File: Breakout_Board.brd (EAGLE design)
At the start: 100 x 80 mm, 93 parts, among them IC101 AD8620R, IC102 AD8620R, IC103 ADE7880, IC104 RH/H6, IC105 7805TV, Q101 16M384, U101 ADR512ARTZ-REEL7, U102 SI8640BD-B-IS, U103 SI8641BD-B-IS, X1 231-538/001-000, X101 STL266-04, X103 MKDSN1,5/2-5,08

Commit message: Board layout updated
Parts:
- moved R4 97.7 mm to (21.6, 70.6)
- moved R5 94.2 mm to (38.4, 51.3), turned to 180 degrees
- moved R1 89.8 mm to (10.7, 71.4), turned to 270 degrees
- moved R3 89.1 mm to (16.8, 70.6), turned to 180 degrees
- moved C2 85.0 mm to (49.8, 41.9), turned to 270 degrees
- moved R2 83.2 mm to (42.9, 42.2)
- moved X103 59.3 mm to (96.0, 16.8), turned to 270 degrees
- moved C102 30.5 mm to (17.8, 46.0), turned to 270 degrees
- moved R121 30.4 mm to (20.3, 40.4)
- moved C103 29.5 mm to (25.4, 44.5), turned to 270 degrees
- moved R112 25.4 mm to (16.0, 40.4), turned to 180 degrees
- moved R106 25.2 mm to (10.4, 40.9)
- moved C109 20.3 mm to (49.5, 21.6)
- moved R127 18.8 mm to (42.9, 23.6), turned to 270 degrees
- moved C105 18.4 mm to (17.8, 64.8), turned to 270 degrees
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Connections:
- net IAN: now also C2.2, R1.2, R3.2, X1.L2; no longer C109.2, R106.1, R112.2, X1.L8
- net IAP: now also C2.1, R2.2; no longer C109.1, R127.2
- net IBN: now also C107.2, R104.2, R110.2, X1.L3; no longer C108.2, R105.1, R111.2, X1.L6
- net IBP: now also C107.1, R125.2; no longer C108.1, R126.2
- net ICN: now also C108.2, R105.2, R111.2, X1.L6; no longer C107.2, R104.1, R110.2, X1.L4
- net ICP: now also C108.1, R126.2; no longer C107.1, R125.2
- net INN: now also C109.2, R106.1, R112.2, X1.L7; no longer C2.2, R1.1, R3.2, X1.L2
- net INP: now also C109.1, R127.2; no longer C2.1, R2.2
- net IN_I1: now also IC102.3, R104.1, X1.L4; no longer IC101.3, R104.2, X1.L3
- net IN_I2: now also R105.1; no longer R105.2
- net IN_I3: now also IC101.3, X1.L8; no longer IC102.3, X1.L7
- net N$18: now also IC101.1; no longer IC102.1
- net N$19: now also IC102.2; no longer IC101.2
- net N$21: now also IC102.1; no longer IC101.1
- net N$23: now also R1.1; no longer R1.2
- net N$29: now also IC101.2; no longer IC102.2
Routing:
- net VCC: track 48.7 -> 129.1 mm, vias 0 -> 3
- net INN: track 0.00 -> 63.5 mm, vias 0 -> 2
- net ICN: track 2.96 -> 62.3 mm, vias 0 -> 2
- net IAN: track 16.1 -> 70.2 mm, vias 0 -> 2
- net GND: track 37.7 -> 90.6 mm, vias 0 -> 5
- net N$22: track 0.00 -> 50.3 mm, vias 0 -> 2
- net IBN: track 25.7 -> 72.2 mm, vias 0 -> 2
- net N$21: track 2.28 -> 43.7 mm, vias 0 -> 2
- net GND_P: track 63.7 -> 24.4 mm, vias 0 -> 3
- net N$16: track 4.38 -> 41.3 mm, vias 0 -> 2
- net N$18: track 7.00 -> 40.9 mm, vias 0 -> 2
- net VCC_P: track 41.9 -> 10.5 mm, vias 0 -> 2
- net IN_I2: track 0.00 -> 24.5 mm
- net N$46: track 23.5 -> 0.00 mm
- net N$23: track 0.00 -> 22.7 mm, vias 0 -> 2
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- added copper zone on layer 1, net VCC
- added copper zone on layer 1, net VEE

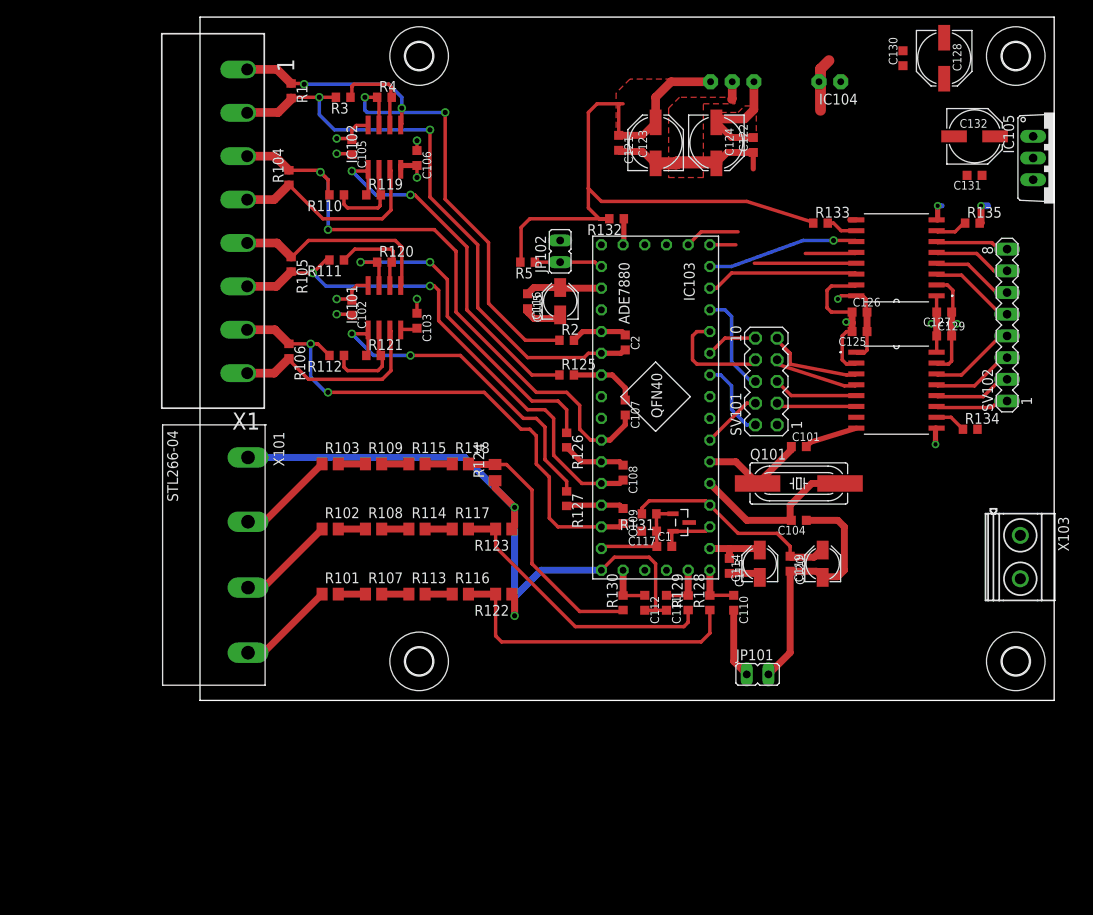
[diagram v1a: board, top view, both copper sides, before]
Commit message: Board layout finished without checking DRC
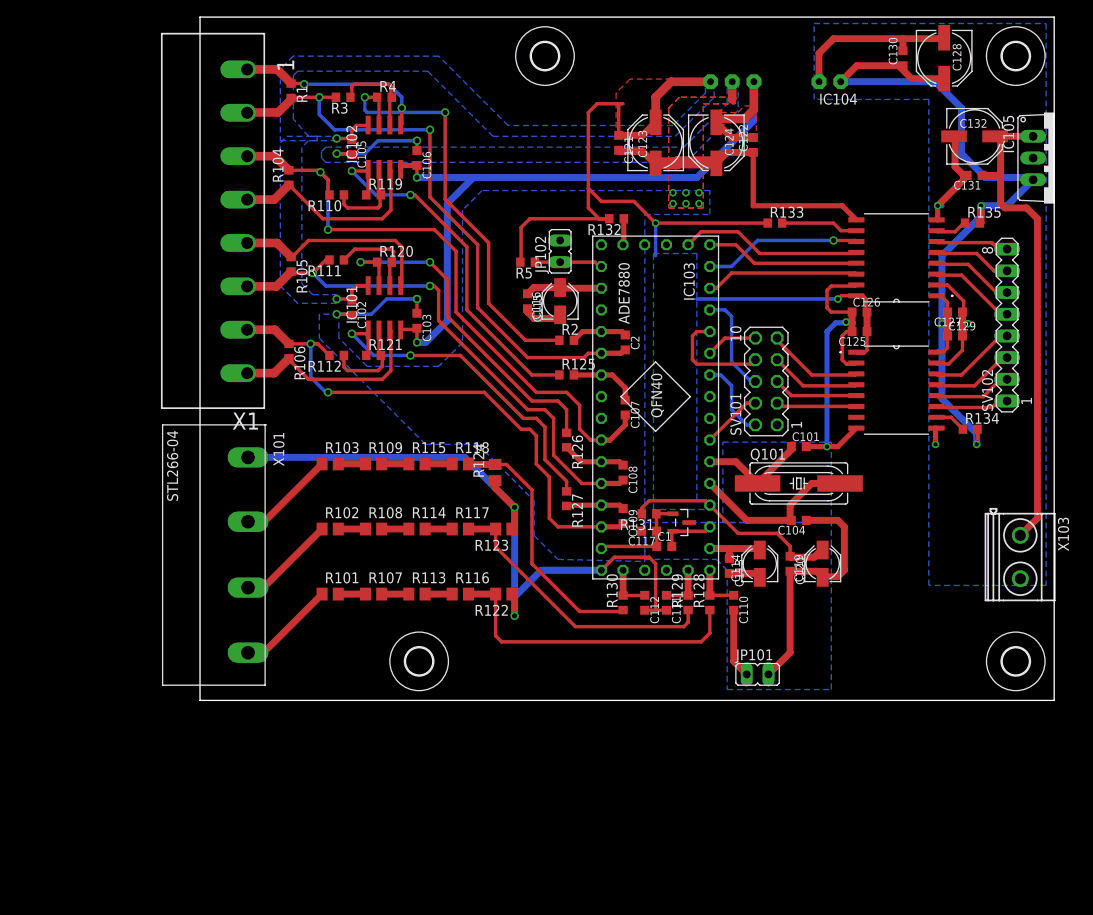
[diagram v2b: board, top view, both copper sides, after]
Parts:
- moved U$3 14.7 mm to (40.4, 75.4)
- moved R133 5.33 mm to (67.3, 55.9)
- moved C127 1.27 mm to (88.4, 45.5)
- moved C129 1.27 mm to (88.4, 42.7)
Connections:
- net GND: now also C117.2
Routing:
- net VCC_P: track 10.5 -> 96.8 mm, vias 2 -> 3
- net VEE: track 19.5 -> 90.3 mm, vias 1 -> 2
- net N$46: track 0.00 -> 57.5 mm
- net GND: track 90.6 -> 142.9 mm, vias 5 -> 12
- net GND_P: track 24.4 -> 48.9 mm
- net VCC: track 129.1 -> 144.4 mm, vias 3 -> 4
- net !SS: track 12.5 -> 21.4 mm
- net N$42: track 3.71 -> 9.04 mm
- net MOSI: track 15.0 -> 18.0 mm
- net MISO: track 17.7 -> 18.5 mm
- added copper zone on layer 16, net GND
- added copper zone on layer 16, net GND_P
- added copper zone on layer 16, net VCC

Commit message: First official release!
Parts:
- R1, R104, R105, R106: value 0R01 -> 4R7
- R110, R111, R112, R3: value 150R -> 6k49
- R119, R120, R121, R4: value 221k -> 2k21
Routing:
- net VN: track 90.7 -> 104.3 mm, vias 2 -> 3
- net GND: track 142.9 -> 136.6 mm
- net N$9: track 33.3 -> 35.8 mm
- net GND_P: vias 3 -> 8
- added copper zone on layer 1, net GND_P
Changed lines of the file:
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@@
 </class>
 <class number="1" name="HighU" width="0" drill="0">
-<clearance class="0" value="2"/>
+<clearance class="0" value="0.0254"/>
 </class>
 <class number="2" name="HIghI" width="0" drill="0">
-<clearance class="0" value="2"/>
+<clearance class="0" value="0.0254"/>
 <clearance class="1" value="2"/>
 </class>
@@
 </class>
 </classes>
-<designrules name="platinenbelichter">
+<designrules name="platinenbelichter *">
 <description language="de">&lt;b&gt;EAGLE Design Rules&lt;/b&gt;
 &lt;p&gt;
@@
 <param name="mtCopper" value="0.035mm 0.035mm 0.035mm 0.035mm 0.035mm 0.035mm 0.035mm 0.035mm 0.035mm 0.035mm 0.035mm 0.035mm 0.035mm 0.035mm 0.035mm 0.035mm"/>
 <param name="mtIsolate" value="1.5mm 0.15mm 0.2mm 0.15mm 0.2mm 0.15mm 0.2mm 0.15mm 0.2mm 0.15mm 0.2mm 0.15mm 0.2mm 0.15mm 0.2mm"/>
-<param name="mdWireWire" value="0.5mm"/>
-<param name="mdWirePad" value="0.5mm"/>
-<param name="mdWireVia" value="0.5mm"/>
-<param name="mdPadPad" value="0.5mm"/>
-<param name="mdPadVia" value="0.5mm"/>
-<param name="mdViaVia" value="0.5mm"/>
+<param name="mdWireWire" value="6mil"/>
+<param name="mdWirePad" value="6mil"/>
+<param name="mdWireVia" value="6mil"/>
+<param name="mdPadPad" value="6mil"/>
+<param name="mdPadVia" value="6mil"/>
+<param name="mdViaVia" value="6mil"/>
 <param name="mdSmdPad" value="0mil"/>
 <param name="mdSmdVia" value="0mil"/>
@@
 <element name="R124" library="rcl" package="R0805" value="1k" x="34.544" y="26.67" rot="R90"/>
 <element name="R130" library="rcl" package="R0603" value="1k" x="49.53" y="11.43" rot="R90"/>
-<element name="R104" library="rcl" package="R0603" value="0R01" x="10.414" y="61.214" rot="R90"/>
+<element name="R104" library="rcl" package="R0603" value="4R7" x="10.414" y="61.214" rot="R90"/>
 <element name="R107" library="rcl" package="R0805" value="162k" x="20.32" y="12.446"/>
 <element name="R125" library="rcl" package="R0603" value="1k" x="42.926" y="38.1"/>
-<element name="R110" library="rcl" package="R0603" value="150R" x="16.002" y="59.182" rot="R180"/>
-<element name="R119" library="rcl" package="R0603" value="221k" x="20.32" y="59.182"/>
-<element name="R105" library="rcl" package="R0603" value="0R01" x="10.668" y="51.054" rot="R270"/>
+<element name="R110" library="rcl" package="R0603" value="6k49" x="16.002" y="59.182" rot="R180"/>
+<element name="R119" library="rcl" package="R0603" value="2k21" x="20.32" y="59.182"/>
+<element name="R105" library="rcl" package="R0603" value="4R7" x="10.668" y="51.054" rot="R270"/>
 <element name="R126" library="rcl" package="R0603" value="1k" x="42.926" y="30.48" rot="R270"/>
-<element name="R111" library="rcl" package="R0603" value="150R" x="16.002" y="51.562" rot="R180"/>
-<element name="R120" library="rcl" package="R0603" value="221k" x="21.59" y="51.308"/>
-<element name="R106" library="rcl" package="R0603" value="0R01" x="10.414" y="40.894" rot="R270"/>
+<element name="R111" library="rcl" package="R0603" value="6k49" x="16.002" y="51.562" rot="R180"/>
+<element name="R120" library="rcl" package="R0603" value="2k21" x="21.59" y="51.308"/>
+<element name="R106" library="rcl" package="R0603" value="4R7" x="10.414" y="40.894" rot="R270"/>
 <element name="R127" library="rcl" package="R0603" value="1k" x="42.926" y="23.622" rot="R270"/>
-<element name="R112" library="rcl" package="R0603" value="150R" x="16.002" y="40.386" rot="R180"/>
+<element name="R112" library="rcl" package="R0603" value="6k49" x="16.002" y="40.386" rot="R180"/>
 <element name="R113" library="rcl" package="R0805" value="196k" x="25.4" y="12.446"/>
-<element name="R121" library="rcl" package="R0603" value="221k" x="20.32" y="40.386"/>
+<element name="R121" library="rcl" package="R0603" value="2k21" x="20.32" y="40.386"/>
 <element name="R132" library="rcl" package="R0603" value="10k" x="48.768" y="56.388" rot="R180"/>
 <element name="R131" library="rcl" package="R0603" value="2k1" x="52.578" y="21.844" rot="R180"/>
@@
 <element name="U$3" library="holes" package="3,2" value="" x="40.386" y="75.438"/>
 <element name="U$4" library="holes" package="3,2" value="" x="95.504" y="75.438"/>
-<element name="R1" library="rcl" package="R0603" value="0R01" x="10.668" y="71.374" rot="R270"/>
+<element name="R1" library="rcl" package="R0603" value="4R7" x="10.668" y="71.374" rot="R270"/>
 <element name="R2" library="rcl" package="R0603" value="1k" x="42.926" y="42.164"/>
 <element name="C2" library="rcl" package="C0603K" value="2n2" x="49.784" y="41.91" rot="R270"/>
-<element name="R3" library="rcl" package="R0603" value="150R" x="16.764" y="70.612" rot="R180"/>
-<element name="R4" library="rcl" package="R0603" value="221k" x="21.59" y="70.612"/>
+<element name="R3" library="rcl" package="R0603" value="6k49" x="16.764" y="70.612" rot="R180"/>
+<element name="R4" library="rcl" package="R0603" value="2k21" x="21.59" y="70.612"/>
 <element name="X1" library="con-wago_5.08mm" package="P-231-538/001-000" value="231-538/001-000" x="1.524" y="56.134" rot="R180"/>
 <element name="R5" library="rcl" package="R0603" value="10k" x="38.354" y="51.308" rot="R180"/>
@@
 <wire x1="31.43" y1="20.066" x2="34.61" y2="20.066" width="0.8128" layer="1"/>
 <wire x1="34.61" y1="20.066" x2="34.61" y2="17.968" width="0.4064" layer="1"/>
-<wire x1="34.61" y1="17.968" x2="43.942" y2="8.636" width="0.4064" layer="1"/>
-<wire x1="43.942" y1="8.636" x2="56.642" y2="8.636" width="0.4064" layer="1"/>
-<wire x1="56.642" y1="8.636" x2="57.15" y2="9.144" width="0.4064" layer="1"/>
+<wire x1="34.61" y1="17.968" x2="44.704" y2="7.874" width="0.4064" layer="1"/>
 <wire x1="57.15" y1="9.144" x2="57.15" y2="10.58" width="0.4064" layer="1"/>
+<wire x1="44.704" y1="7.874" x2="56.642" y2="7.874" width="0.4064" layer="1"/>
+<wire x1="56.642" y1="7.874" x2="57.15" y2="8.382" width="0.4064" layer="1"/>
+<wire x1="57.15" y1="8.382" x2="57.15" y2="10.58" width="0.4064" layer="1"/>
 </signal>
 <signal name="N$11" class="1">
@@
 <wire x1="34.544" y1="25.72" x2="34.544" y2="24.892" width="0.8128" layer="1"/>
 <wire x1="34.544" y1="24.892" x2="36.83" y2="22.606" width="0.8128" layer="1"/>
-<wire x1="54.61" y1="10.555" x2="62.484" y2="10.555" width="0" layer="19" extent="1-1"/>
+<wire x1="54.61" y1="10.555" x2="54.61" y2="9.144" width="0.4064" layer="1"/>
+<via x="54.61" y="9.144" extent="1-16" drill="0.6" shape="octagon"/>
+<wire x1="54.61" y1="9.144" x2="54.61" y2="8.636" width="0.4064" layer="16"/>
+<wire x1="54.61" y1="8.636" x2="60.198" y2="3.048" width="0.4064" layer="16"/>
+<wire x1="60.198" y1="3.048" x2="64.008" y2="3.048" width="0.4064" layer="16"/>
 </signal>
 <signal name="N$5" class="1">
@@
 <wire x1="25.4" y1="64.375" x2="25.4" y2="65.532" width="0.4064" layer="1"/>
 <via x="25.4" y="65.532" extent="1-16" drill="0.6"/>
-<wire x1="25.4" y1="65.532" x2="25.654" y2="65.532" width="0.4064" layer="16"/>
 <wire x1="17.78" y1="63.895" x2="17.78" y2="64.008" width="0.4064" layer="1"/>
 <wire x1="17.78" y1="64.008" x2="16.002" y2="64.008" width="0.4064" layer="1"/>
@@
 <wire x1="74.675" y1="29.718" x2="76.834" y2="31.877" width="0.6096" layer="1"/>
 <wire x1="16.002" y1="64.008" x2="19.304" y2="64.008" width="0.4064" layer="16"/>
-<wire x1="19.304" y1="64.008" x2="20.828" y2="65.532" width="0.4064" layer="16"/>
-<wire x1="20.828" y1="65.532" x2="25.4" y2="65.532" width="0.4064" layer="16"/>
 <wire x1="16.002" y1="45.212" x2="20.066" y2="45.212" width="0.4064" layer="16"/>
 <wire x1="20.066" y1="45.212" x2="21.844" y2="46.99" width="0.4064" layer="16"/>
@@
 <wire x1="75.183" y1="57.912" x2="76.834" y2="56.261" width="0.6096" layer="1"/>
 <contactref element="C117" pad="2"/>
+<wire x1="25.4" y1="65.532" x2="25.4" y2="64.77" width="0.4064" layer="16"/>
 <wire x1="75.946" y1="44.196" x2="75.634" y2="44.3" width="0" layer="19" extent="16-16"/>
 <wire x1="51.703" y1="19.812" x2="55.231" y2="19.662" width="0" layer="19" extent="1-1"/>
@@
 <wire x1="86.982" y1="77.584" x2="86.868" y2="77.47" width="0.8128" layer="1"/>
 <wire x1="82.296" y1="76.059" x2="82.296" y2="77.47" width="0.8128" layer="1"/>
+<polygon width="0.4064" layer="1">
+<vertex x="85.344" y="70.358"/>
+<vertex x="85.344" y="67.818"/>
+<vertex x="93.726" y="67.818"/>
+<vertex x="93.726" y="70.612"/>
+<vertex x="91.44" y="72.898"/>
+<vertex x="91.186" y="72.898"/>
+<vertex x="88.646" y="70.358"/>
+</polygon>
+<via x="86.106" y="69.596" extent="1-16" drill="0.6"/>
+<via x="86.106" y="68.326" extent="1-16" drill="0.6"/>
+<via x="90.424" y="70.612" extent="1-16" drill="0.6"/>
+<via x="91.44" y="71.882" extent="1-16" drill="0.6"/>
+<via x="92.456" y="70.612" extent="1-16" drill="0.6"/>
 <wire x1="88.392" y1="65.926" x2="88.278" y2="66.04" width="0" layer="19" extent="1-1"/>
 <wire x1="89.803" y1="61.468" x2="89.408" y2="61.468" width="0" layer="19" extent="1-1"/>
@@
 <wire x1="33.782" y1="46.482" x2="33.782" y2="53.594" width="0.4064" layer="1"/>
 <wire x1="33.782" y1="53.594" x2="28.702" y2="58.674" width="0.4064" layer="1"/>
-<wire x1="28.702" y1="58.674" x2="28.702" y2="68.834" width="0.4064" layer="1"/>
-<via x="28.702" y="68.834" extent="1-16" drill="0.6"/>
-<wire x1="28.702" y1="68.834" x2="19.558" y2="68.834" width="0.4064" layer="16"/>
-<wire x1="19.558" y1="68.834" x2="19.304" y2="69.088" width="0.4064" layer="16"/>
-<wire x1="19.304" y1="69.088" x2="19.304" y2="70.612" width="0.4064" layer="16"/>
+<wire x1="28.702" y1="58.674" x2="28.702" y2="68.326" width="0.4064" layer="1"/>
+<via x="28.702" y="68.326" extent="1-16" drill="0.6"/>
+<wire x1="28.702" y1="68.326" x2="19.558" y2="68.326" width="0.4064" layer="16"/>
+<wire x1="19.558" y1="68.326" x2="19.304" y2="68.58" width="0.4064" layer="16"/>
+<wire x1="19.304" y1="68.58" x2="19.304" y2="70.612" width="0.4064" layer="16"/>
 <via x="19.304" y="70.612" extent="1-16" drill="0.6"/>
 <wire x1="19.304" y1="70.612" x2="20.74" y2="70.612" width="0.4064" layer="1"/>

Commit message: A1 schematic and layout
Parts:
- removed C102, C103, C105, C106: 220n, rcl:C0603K
- removed C107, C108, C109: 2n2, rcl:C0603K
- removed C122: (no value), rcl:C0603K
- removed C124: 47u, rcl:PANASONIC_D
- removed IC101, IC102: AD8620R, analog-devices:SO8
- removed IC104: RH/H6, recom_own:RH/H6
- removed R104, R105, R106: 4R7, rcl:R0603
- removed R110, R111, R112: 6k49, rcl:R0603
- removed R119, R120, R121: 2k21, rcl:R0603
- removed R125, R126, R127: 1k, rcl:R0603
- added C3, C4, C5, C6, C7, C8, C9: 2n2, rcl:C0603K
- added IC1: RH-0505S/H6, recom_own:RH/H6
- added R10, R11, R14, R15, R18, R6, R7: 2R7, rcl:R0805
- added R12, R13, R16, R17, R8, R9: 150R, rcl:R0805
- added R19, R20, R21, R22, R23, R24, R25: 1k, rcl:R0603
- R1: value 4R7 -> 2R7; device rcl:R0603 -> rcl:R0805
- R3: value 6k49 -> 150R; device rcl:R0603 -> rcl:R0805
- R4: value 2k21 -> 150R; device rcl:R0603 -> rcl:R0805
- moved C2 44.0 mm to (17.8, 72.1), turned to 180 degrees
- moved R2 41.1 mm to (17.8, 74.7)
- moved X103 24.4 mm to (96.0, 41.1)
- moved C125 16.5 mm to (68.1, 56.9)
- moved U102 16.2 mm to (74.2, 50.8)
- moved C126 16.1 mm to (68.1, 58.7)
- moved C129 15.9 mm to (80.8, 56.6)
- moved SV102 15.7 mm to (86.4, 57.4)
- moved C127 15.2 mm to (80.8, 58.7)
- moved R134 15.0 mm to (86.4, 46.2)
- moved U$3 14.7 mm to (25.7, 75.4)
- moved SV101 14.7 mm to (62.5, 51.6)
- moved U103 14.7 mm to (74.2, 64.5)
- moved C1 14.1 mm to (51.1, 31.8)
- moved C110 14.1 mm to (59.2, 25.1)
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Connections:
- removed net AGND: C113.2, C114.-
- removed net DGND: C115.2, C116.-
- removed net IN_I1: IC102.3, R104.1, X1.L4
- removed net IN_I2: IC101.5, R105.1, X1.L5
- removed net IN_I3: IC101.3, R106.2, X1.L8
- removed net N$16: IC101.7, R120.1, R126.1
- removed net N$17: IC102.6, R3.1, R4.2
- removed net N$18: IC101.1, R121.1, R127.1
- removed net N$19: IC102.2, R110.1, R119.2
- removed net N$21: IC102.1, R119.1, R125.1
- removed net N$22: IC102.7, R2.1, R4.1
- removed net N$23: IC102.5, R1.1, X1.L1
- removed net N$24: IC101.6, R111.1, R120.2
- removed net N$29: IC101.2, R112.1, R121.2
- removed net VEE: C103.2, C106.2, C122.2, C124.-, IC101.4, IC102.4, IC104.P$3
- new net INH: R15.2, R16.2, R24.1, X1.L7
- new net INL: R17.1, R18.1, R25.1, X1.L8
- new net L1H: R1.2, R2.1, R3.2, X1.L1
- new net L1L: R19.1, R4.1, R6.1, X1.L2
- new net L2H: R20.1, R7.2, R8.2, X1.L3
- new net L2L: R10.1, R21.1, R9.1, X1.L4
- new net L3H: R11.2, R12.2, R22.1, X1.L5
- new net L3L: R13.1, R14.1, R23.1, X1.L6
- net GND: now also C113.2, C114.-, C115.2, C116.-, C2.2, C3.1, C4.2, C5.1, C6.2, C7.1, C8.2, C9.1, IC1.P$3, R1.1, R10.2, R11.1, R12.1, R13.2, R14.2, R15.1, R16.1, R17.2, R18.2, R3.1, R4.2, R6.2, R7.1, R8.1, R9.2; no longer C102.2, C103.1, C105.2, C106.1, C122.1, C124.+, IC104.P$4
- net GND_P: now also IC1.P$2; no longer IC104.P$2
- net IAN: now also C3.2, R19.2; no longer C2.2, R1.2, R3.2, X1.L2
- net IBN: now also C5.2, R21.2; no longer C107.2, R104.2, R110.2, X1.L3
- net IBP: now also C4.1, R20.2; no longer C107.1, R125.2
- net ICN: now also C7.2, R23.2; no longer C108.2, R105.2, R111.2, X1.L6
- net ICP: now also C6.1, R22.2; no longer C108.1, R126.2
- net INN: now also C9.2, R25.2; no longer C109.2, R106.1, R112.2, X1.L7
- net INP: now also C8.1, R24.2; no longer C109.1, R127.2
- net VCC: now also IC1.P$5; no longer C102.1, C105.1, IC101.8, IC102.8, IC104.P$5
- net VCC_P: now also IC1.P$1; no longer IC104.P$1
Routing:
- net VEE: track 90.3 -> 0.00 mm, vias 2 -> 0
- net N$22: track 50.3 -> 0.00 mm, vias 2 -> 0
- net N$21: track 43.7 -> 0.00 mm, vias 2 -> 0
- net N$16: track 41.3 -> 0.00 mm, vias 2 -> 0
- net N$18: track 40.9 -> 0.00 mm, vias 2 -> 0
- net IBN: track 72.2 -> 33.0 mm, vias 2 -> 0
- net IAN: track 70.2 -> 32.9 mm, vias 2 -> 0
- net VCC: track 144.4 -> 108.6 mm, vias 4 -> 2
- net INN: track 63.5 -> 28.9 mm, vias 2 -> 0
- net ICN: track 62.3 -> 31.1 mm, vias 2 -> 0
- net IAP: track 6.59 -> 34.5 mm
- net N$46: track 57.5 -> 30.6 mm
- net ICP: track 7.47 -> 32.0 mm
- net IN_I2: track 24.5 -> 0.00 mm
- net IN_I1: track 24.4 -> 0.00 mm
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- removed copper zone on layer 1, net GND_P
- removed copper zone on layer 1, net VCC
- removed copper zone on layer 1, net VEE
